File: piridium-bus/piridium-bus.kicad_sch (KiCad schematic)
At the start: 81 parts, among them J1 EPS, J2 MODEM UART, J3 INHIBITS, J4 ANT, J5 PAYLOAD, Q1 DMP3015LSSQ, Q2 Si4186DY, Q3 DMP3015LSSQ, Q4 Si4186DY, Q5 DMP3015LSSQ, Q6 DMP3015LSSQ, Q7 2N7002, Q8 DMP3015LSSQ, U1 LM1117-3.3, U2 TPS54394RSAR, U3 MAX6369, U4 74HC126, U5 INA180A3, U6 DS3232M, U7 INA180A3, U8 MCP3208

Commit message: ngl not sure what I did here
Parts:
- R18, R19, R21, R4, R8: footprint Resistor_SMD:R_1206_3216Metric -> Resistor_SMD:R_0805_2012Metric
- U8: footprint (none) -> Package_SO:SOIC-16_3.9x9.9mm_P1.27mm
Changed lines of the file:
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@@
     )
     (property "Value" "100K" (id 1) (at 45.72 46.99 90))
-    (property "Footprint" "Resistor_SMD:R_1206_3216Metric" (id 2) (at 43.942 46.99 90)
+    (property "Footprint" "Resistor_SMD:R_0805_2012Metric" (id 2) (at 43.942 46.99 90)
       (effects (font (size 1.27 1.27)) hide)
     )
@@
     )
     (property "Value" "100K" (id 1) (at 86.36 39.37 90))
-    (property "Footprint" "Resistor_SMD:R_1206_3216Metric" (id 2) (at 84.582 39.37 90)
+    (property "Footprint" "Resistor_SMD:R_0805_2012Metric" (id 2) (at 84.582 39.37 90)
       (effects (font (size 1.27 1.27)) hide)
     )
@@
       (effects (font (size 1.27 1.27)) (justify left))
     )
-    (property "Footprint" "" (id 2) (at 304.8 113.03 0)
+    (property "Footprint" "Package_SO:SOIC-16_3.9x9.9mm_P1.27mm" (id 2) (at 304.8 113.03 0)
       (effects (font (size 1.27 1.27)) hide)
     )
@@
     (property "Reference" "R18" (id 0) (at 223.52 27.94 90))
     (property "Value" "100R" (id 1) (at 223.52 30.48 90))
-    (property "Footprint" "Resistor_SMD:R_1206_3216Metric" (id 2) (at 223.52 32.258 90)
+    (property "Footprint" "Resistor_SMD:R_0805_2012Metric" (id 2) (at 223.52 32.258 90)
       (effects (font (size 1.27 1.27)) hide)
     )
@@
     )
     (property "Value" "10K" (id 1) (at 227.33 34.29 90))
-    (property "Footprint" "Resistor_SMD:R_1206_3216Metric" (id 2) (at 229.108 34.29 90)
+    (property "Footprint" "Resistor_SMD:R_0805_2012Metric" (id 2) (at 229.108 34.29 90)
       (effects (font (size 1.27 1.27)) hide)
     )
@@
     )
     (property "Value" "10K" (id 1) (at 234.95 21.59 90))
-    (property "Footprint" "Resistor_SMD:R_1206_3216Metric" (id 2) (at 236.728 21.59 90)
+    (property "Footprint" "Resistor_SMD:R_0805_2012Metric" (id 2) (at 236.728 21.59 90)
       (effects (font (size 1.27 1.27)) hide)
     )
@@
     )
     (path "/199564e9-96da-49ce-aee2-4093db89e0a3"
-      (reference "R4") (unit 1) (value "100K") (footprint "Resistor_SMD:R_1206_3216Metric")
+      (reference "R4") (unit 1) (value "100K") (footprint "Resistor_SMD:R_0805_2012Metric")
     )
     (path "/3a343ae2-b78b-48a5-820b-4441c1fa28dc"
@@
     )
     (path "/4ead0ca1-aaf2-482d-b51c-2ffe077e1536"
-      (reference "R8") (unit 1) (value "100K") (footprint "Resistor_SMD:R_1206_3216Metric")
+      (reference "R8") (unit 1) (value "100K") (footprint "Resistor_SMD:R_0805_2012Metric")
     )
     (path "/cd81d2b7-153f-4170-9e05-8e14f96c2367"
@@
     )
     (path "/59cd26eb-6e63-4857-a984-ee928ccec899"
-      (reference "R18") (unit 1) (value "100R") (footprint "Resistor_SMD:R_1206_3216Metric")
+      (reference "R18") (unit 1) (value "100R") (footprint "Resistor_SMD:R_0805_2012Metric")
     )
     (path "/e6d1af79-d7c7-41f9-85d8-9729ef258901"
-      (reference "R19") (unit 1) (value "10K") (footprint "Resistor_SMD:R_1206_3216Metric")
+      (reference "R19") (unit 1) (value "10K") (footprint "Resistor_SMD:R_0805_2012Metric")
     )
     (path "/b5cc64de-c33d-4294-8351-c594caa2bce6"
@@
     )
     (path "/ea20ca82-5b13-40f2-8490-5e4e92c8de31"
-      (reference "R21") (unit 1) (value "10K") (footprint "Resistor_SMD:R_1206_3216Metric")
+      (reference "R21") (unit 1) (value "10K") (footprint "Resistor_SMD:R_0805_2012Metric")
     )
     (path "/44ac684e-df22-4ba9-b0ef-36d4bf4babc1"

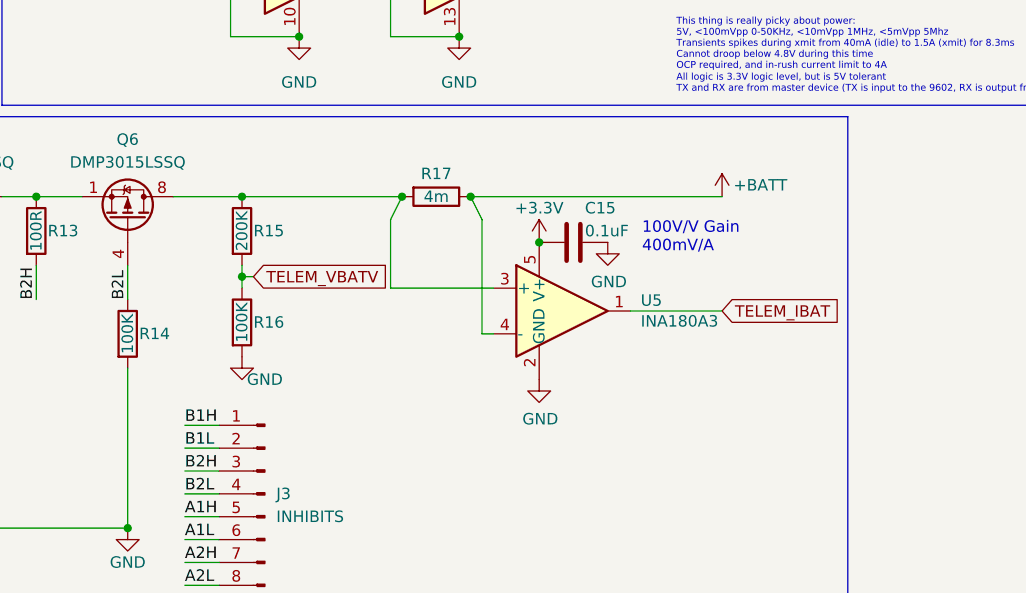
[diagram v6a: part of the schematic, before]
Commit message: route inhibits and some other power path stuff
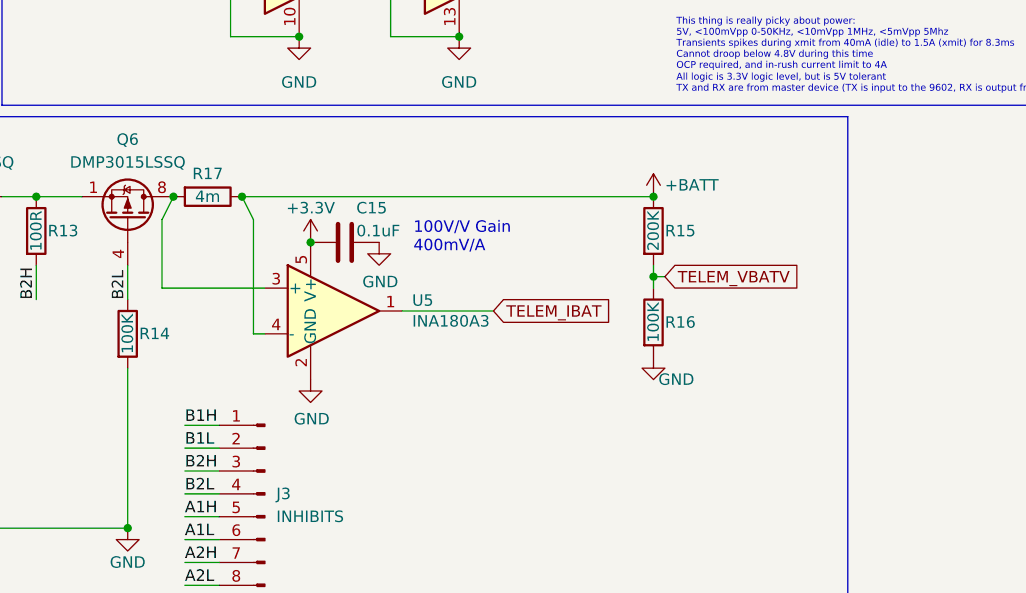
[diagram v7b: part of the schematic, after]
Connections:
- net +BATT: now also R15.1
- net at Q6.5 (D), Q6.6 (D), Q6.7 (D)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: no longer R15.1
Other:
- moved on the sheet: C15, R15, R16, R17, U5

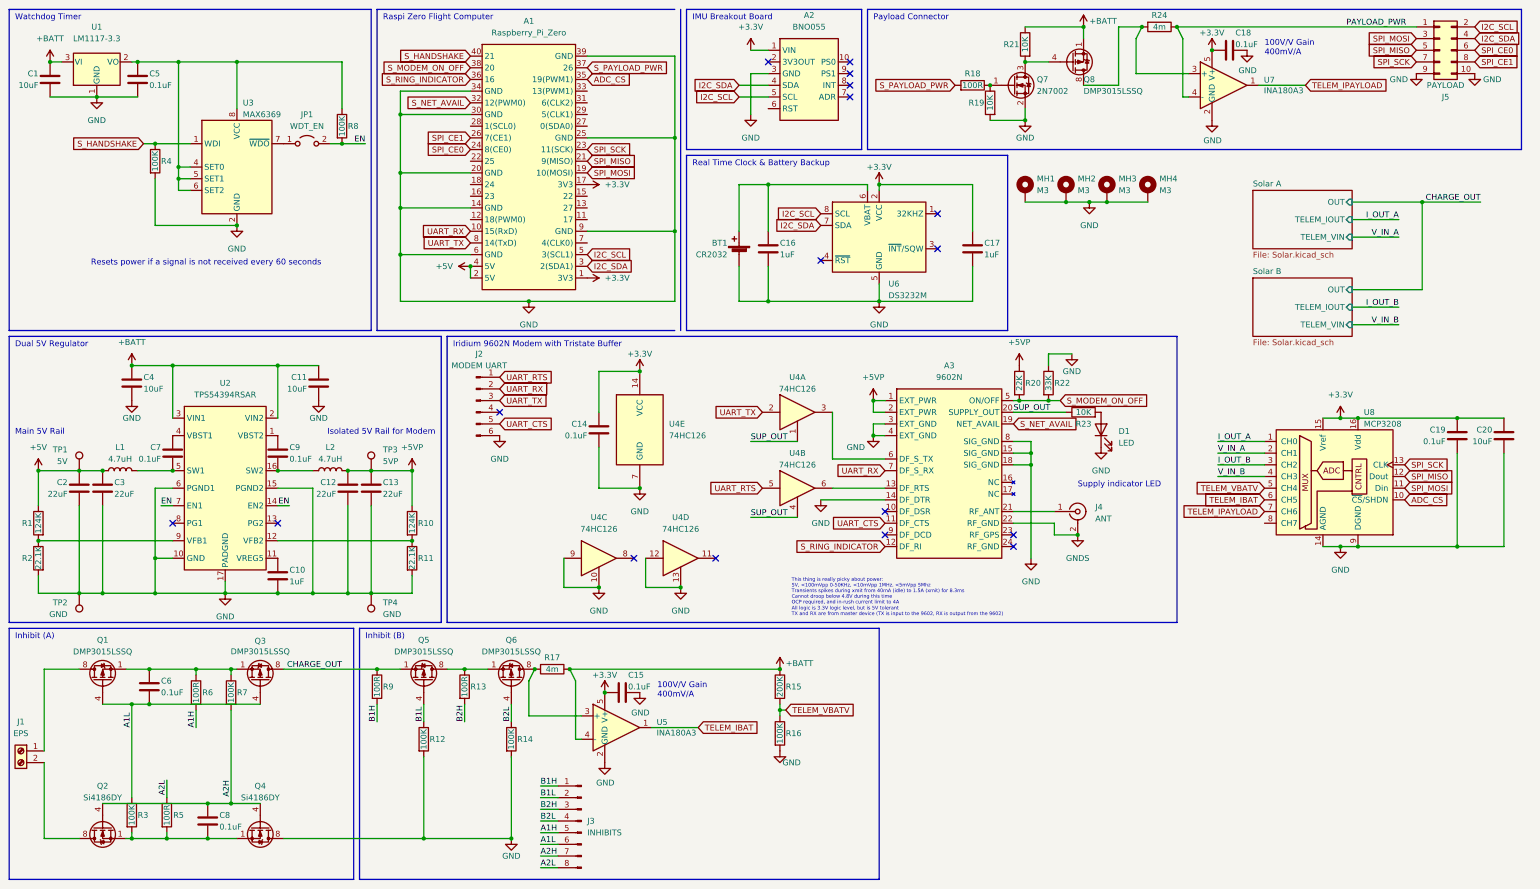
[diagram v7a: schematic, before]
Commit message: route data lines, begin to route MPPT circuitry
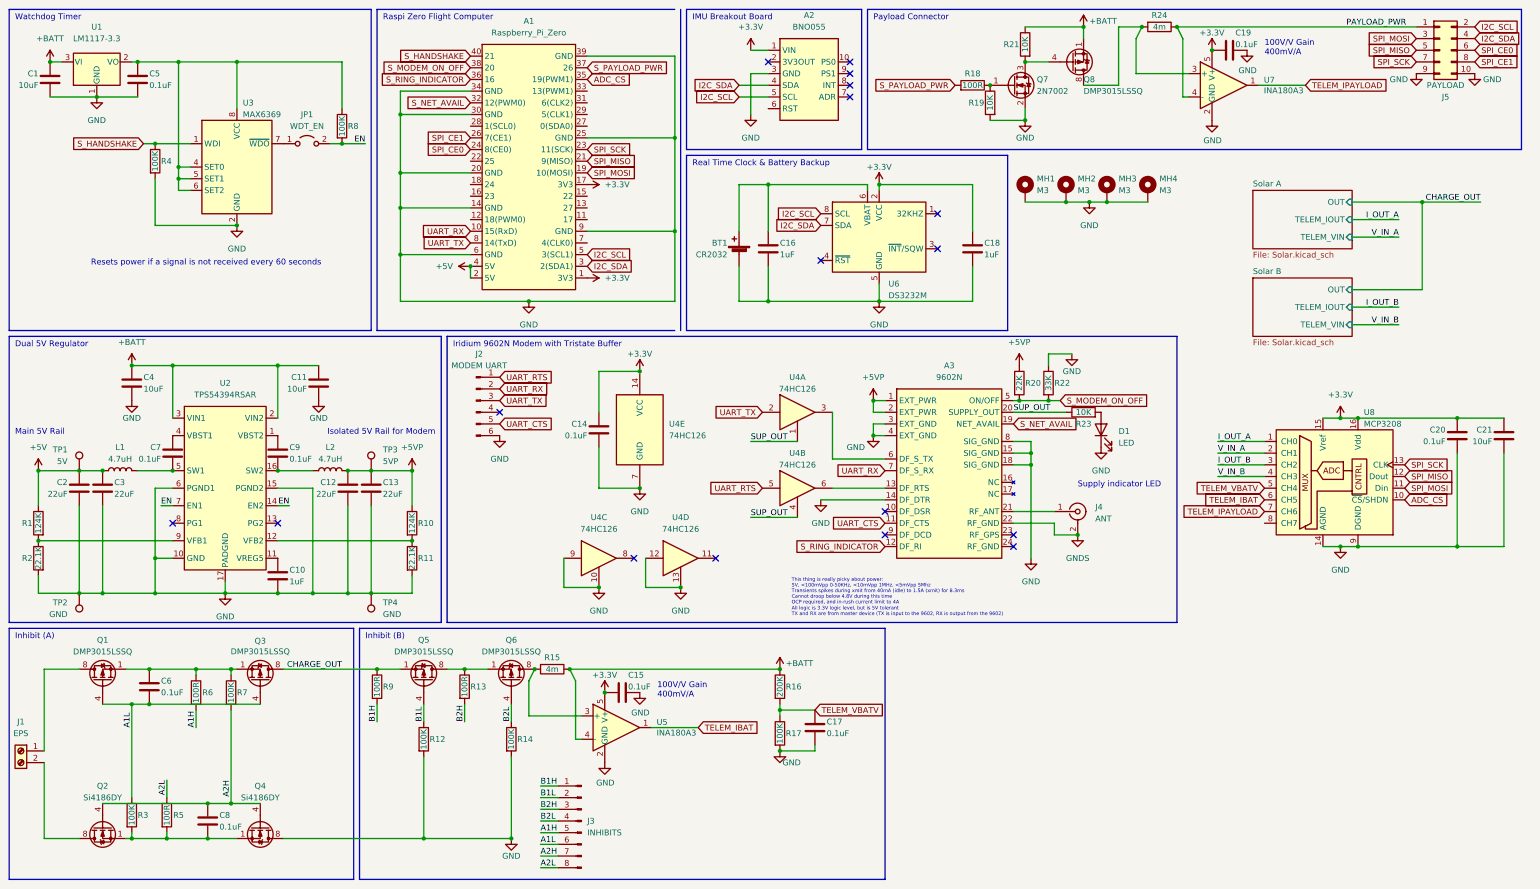
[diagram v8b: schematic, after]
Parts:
- added C17: 0.1uF, Capacitor_SMD:C_0805_2012Metric, symbol Device:C
- renumbered C17 to C18, C18 to C19, C19 to C20, C20 to C21, R17 to R15, R15 to R16, R16 to R17
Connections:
- net GND: now also C17.2
- net TELEM_VBATV: now also C17.1
